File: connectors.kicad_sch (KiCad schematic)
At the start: 28 parts, among them U1 TPS259472A, U6 TPS259472A

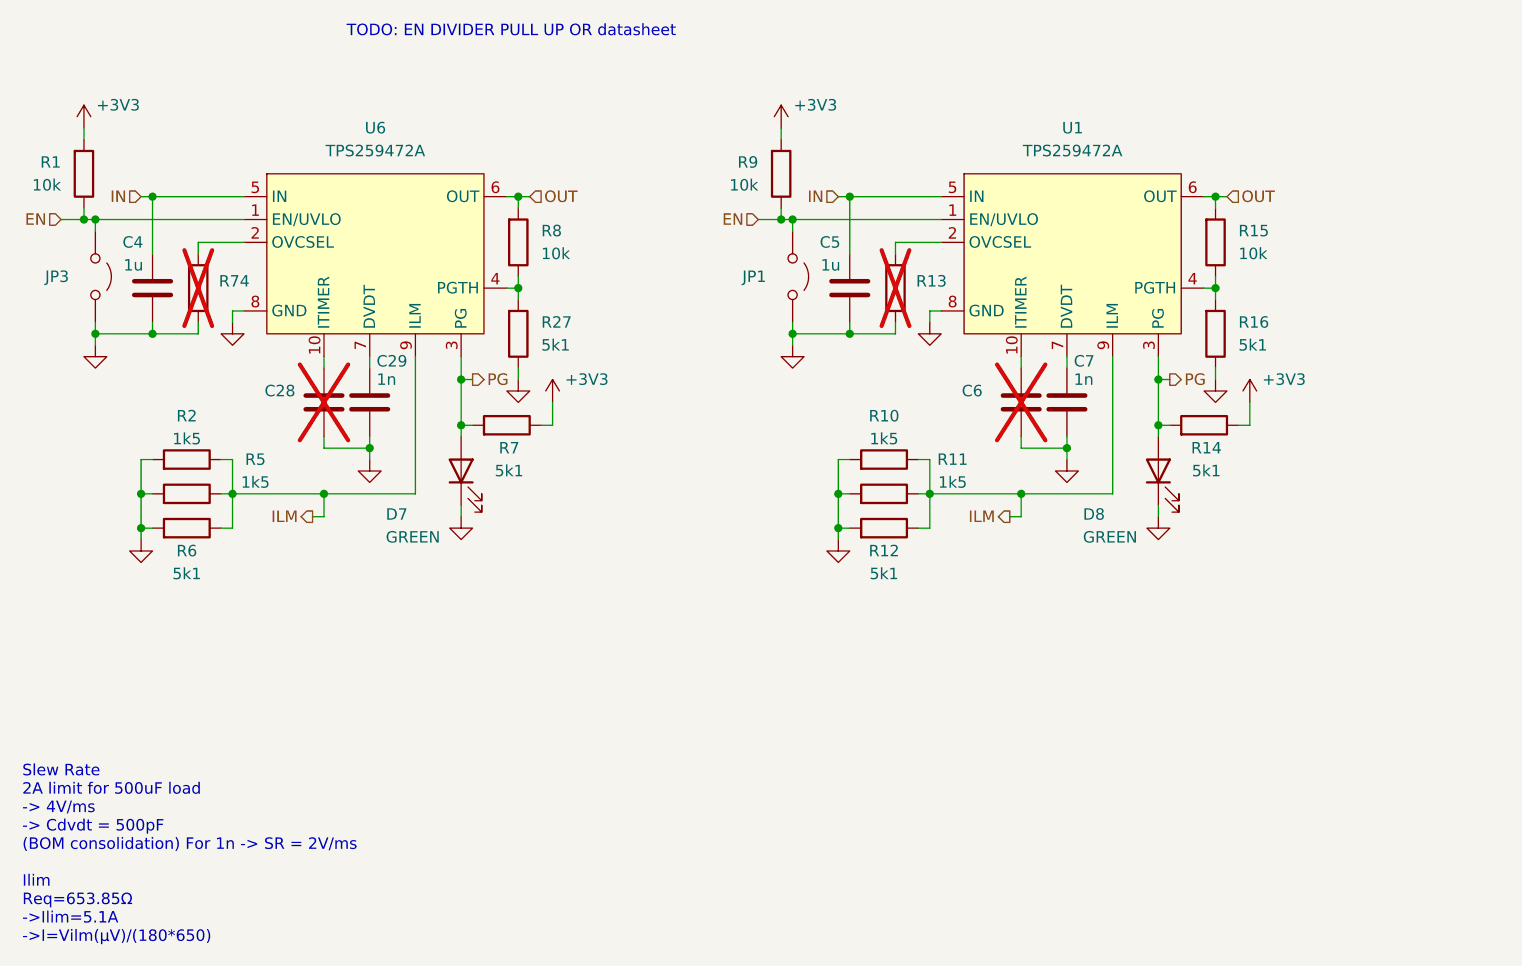
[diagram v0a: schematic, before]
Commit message: schem: update efuse to work as downstream
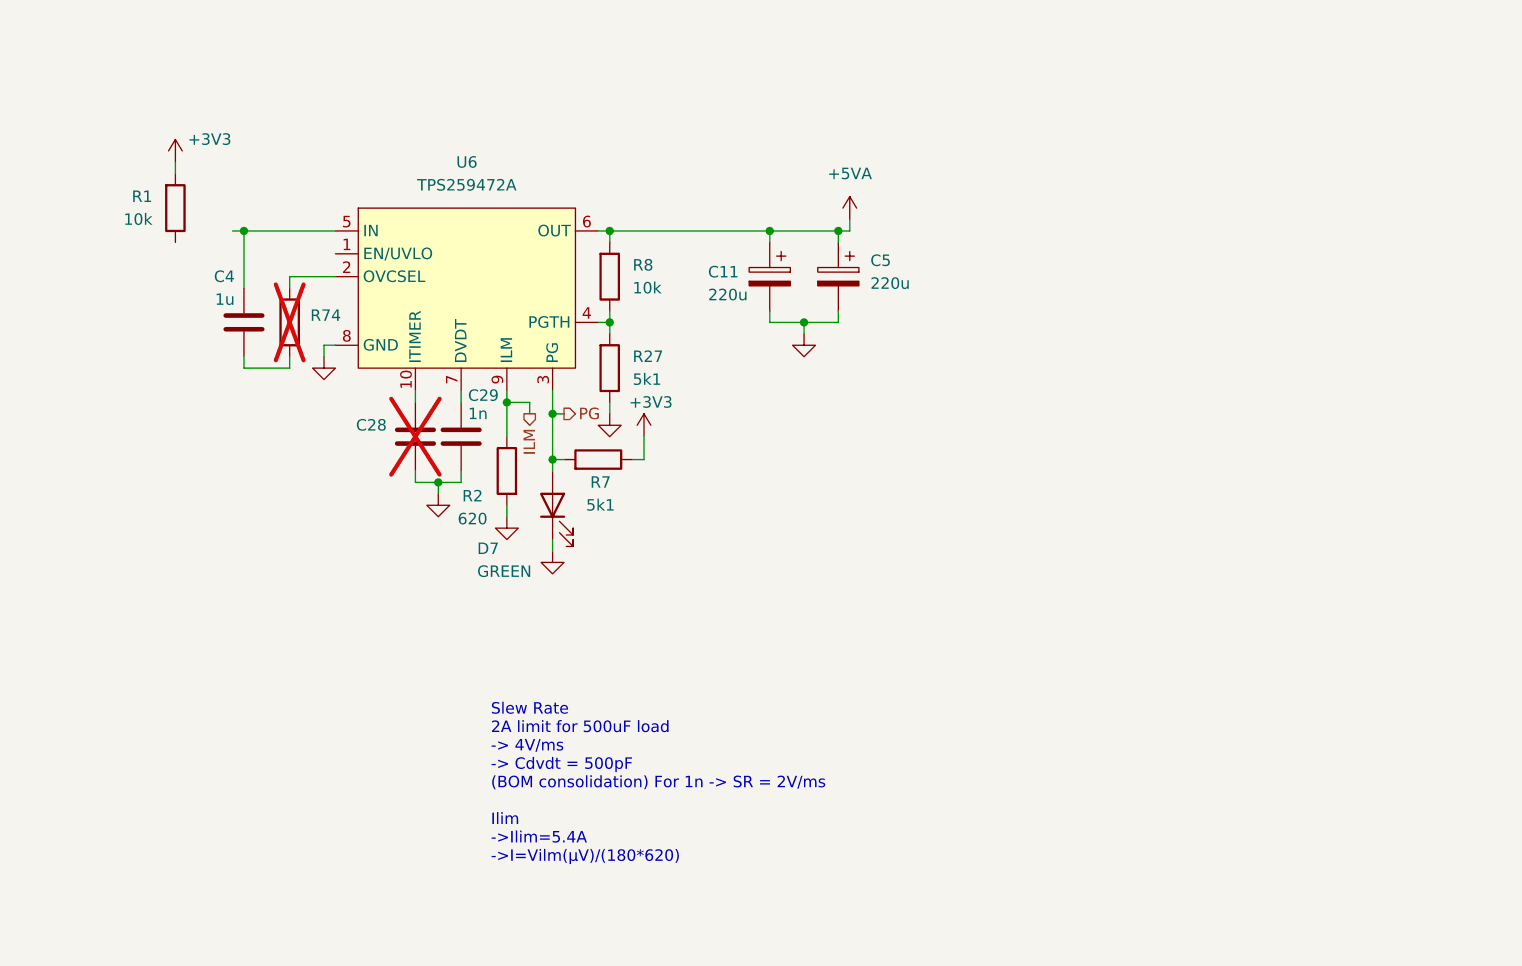
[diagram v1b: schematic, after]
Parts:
- removed C5: 1u, Capacitor_SMD:C_0402_1005Metric, symbol Device:C
- removed C6: C, Capacitor_SMD:C_0402_1005Metric, symbol Device:C
- removed C7: 1n, Capacitor_SMD:C_0402_1005Metric, symbol Device:C
- removed D8: GREEN, LED_SMD:LED_0805_2012Metric, symbol Device:LED
- removed JP1, JP3: Jumper_2_Small_Open, Connector_PinHeader_2.54mm:PinHeader_2x01_P2.54mm_Vertical, symbol Jumper:Jumper_2_Open
- removed R10, R11, R5: 1k5, Resistor_SMD:R_0402_1005Metric, symbol Device:R
- removed R12, R14, R16, R6: 5k1, Resistor_SMD:R_0402_1005Metric, symbol Device:R
- removed R13: R, Resistor_SMD:R_0402_1005Metric, symbol Device:R
- removed R15, R9: 10k, Resistor_SMD:R_0402_1005Metric, symbol Device:R
- removed U1: TPS259472A, GLCS:Texas_RPW0010A_VQFN-HR-10_2x2mm_P0.5mm, symbol GLCS:TPS259472x
- added C11, C5: 220u, Capacitor_SMD:CP_Elec_6.3x7.7, symbol Device:C_Polarized
- R2: value 1k5 -> 620; Basic Y -> X; JLCPCB Part # C25867 -> C4961; Manufacturer Part Number 0402WGF1501TCE -> 0402WGF6200TCE
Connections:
- net GND: now also C11.2, C5.2; no longer C4.1, R74.2
- net EN: no longer names the net of U6.1 (EN/UVLO)
- net EN: no longer R1.1
- net IN: no longer names the net of C4.2, U6.5 (IN)
- net OUT renamed +5VA
- net +5VA: now also C11.1, C5.1
- new net: C4.1, R74.2
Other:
- note added: "Slew Rate 2A limit for 500uF load -> 4V/ms -> Cdvdt = 500pF (BOM consolidation) For 1n -> SR = 2V/ms Ilim ->Ilim=5.4A ->I=Vilm(µV)/(180*620)"
- note removed: "Slew Rate 2A limit for 500uF load -> 4V/ms -> Cdvdt = 500pF (BOM consolidation) For 1n -> SR = 2V/ms Ilim Req=653.85Ω ->Ilim=5.1A ->I=Vilm(µV)/(180*650)"
- note removed: "TODO: EN DIVIDER PULL UP OR datasheet"
- moved on the sheet: C28, C29, C4, D7, R1, R27, R7, R74, R8, U6

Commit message: schem: configure efuse
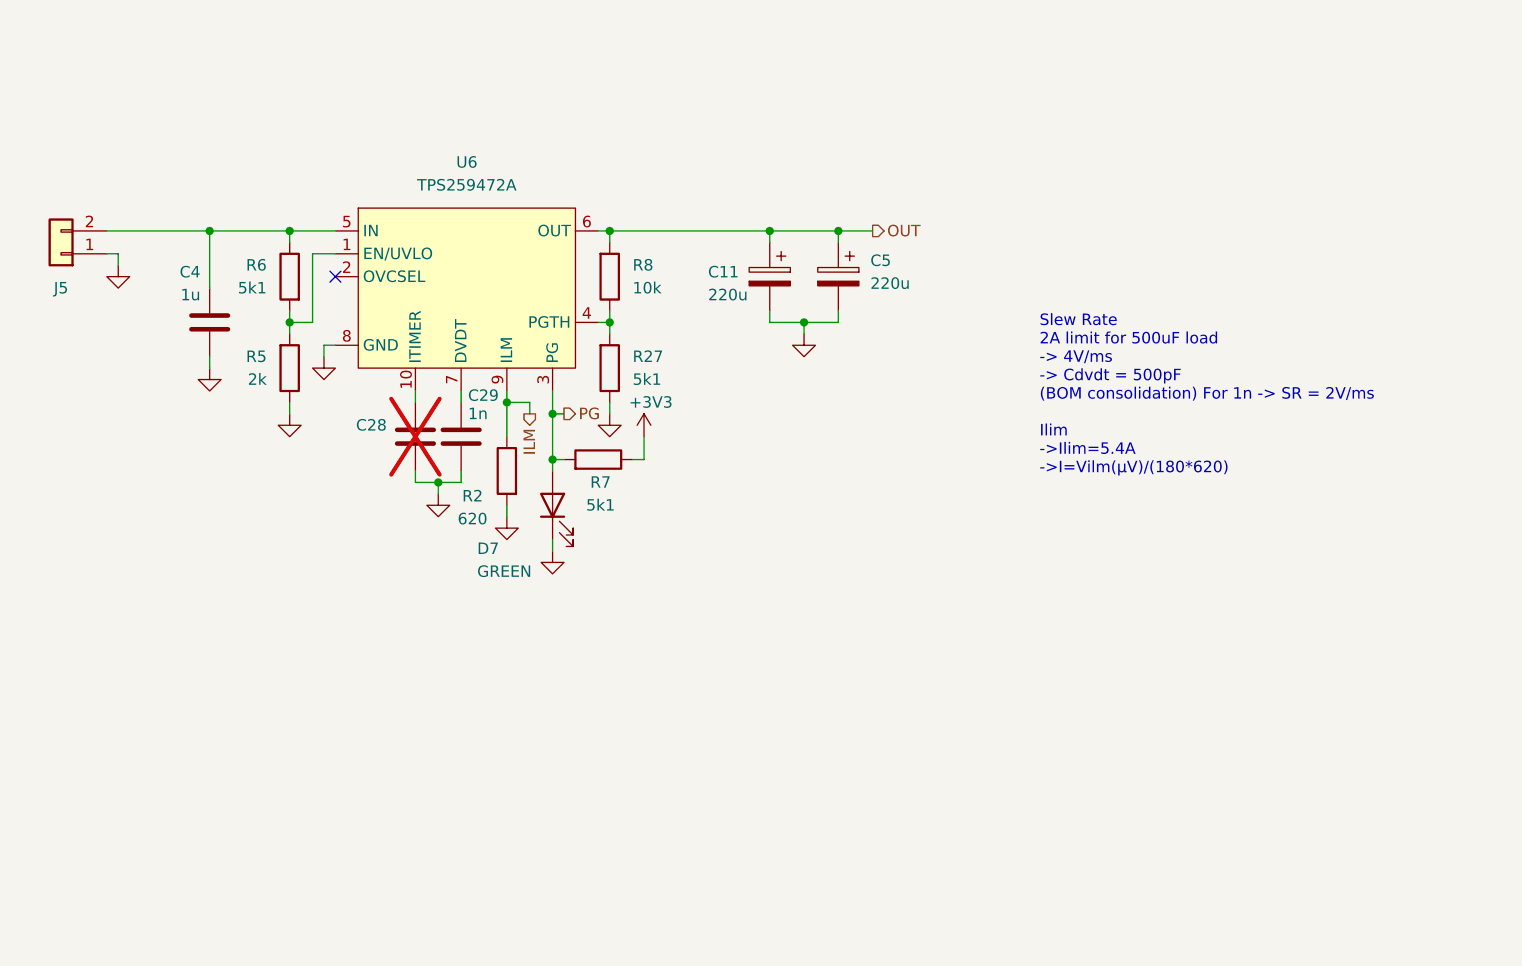
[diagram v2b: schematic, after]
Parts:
- removed R1: 10k, Resistor_SMD:R_0402_1005Metric, symbol Device:R
- removed R74: R, Resistor_SMD:R_0402_1005Metric, symbol Device:R
- added J5: Conn_01x02, Connector_JST:JST_XH_B2B-XH-A_1x02_P2.50mm_Vertical, symbol Connector_Generic:Conn_01x02
- added R5: 2k, Resistor_SMD:R_0402_1005Metric, symbol Device:R
- added R6: 5k1, Resistor_SMD:R_0402_1005Metric, symbol Device:R
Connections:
- net GND: now also C4.1, J5.1 (Pin_1), R5.1
- net at U6.1 (EN/UVLO): now also R5.2, R6.2
- net at C4.2, U6.5 (IN): now also J5.2 (Pin_2), R6.1
- net +5VA renamed OUT
- no-connect marks 0 -> 1
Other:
- moved on the sheet: C4
